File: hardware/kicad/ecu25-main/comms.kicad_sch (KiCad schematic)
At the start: 19 parts, among them J10 Screw_Terminal_RS485, J9 Screw_Terminal_CAN, U11 M95M02-DR, U6 TJA1051T/3, U7 THVD1450

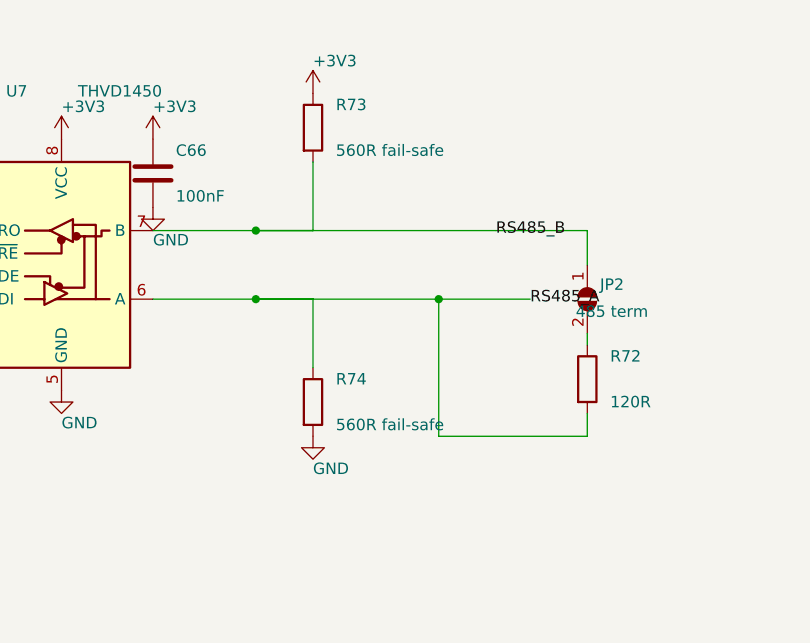
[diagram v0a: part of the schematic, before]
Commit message: Fix SME review findings: 3 critical, 6 major schematic faults
Critical:
- RON pin no longer shorted to GND (R4 moved off C3's column)
- LM2903 MPU comparator +/- inputs unmerged (separate route columns)
- Supercap charge diode D70 un-reversed (anode to +3V3)

Major:
- Buck UVLO divider restored (stray EN stub ended on C3 column = EN
  tied to +24V; stub removed)
- RS485 fail-safe bias polarity corrected (pull-up A, pull-down B)
- U8 spare op-amp unit placed and tied off (was floating on VREF die)
- Heartbeat LED DS1 un-reversed
- VREF_MID buffer dual feedback added (R93 DC path + C93 AC path)
- D80 value SMBJ33A -> SMBJ33CA (bidirectional, matches symbol)

Added netlist-level sweep check (shorted 2-pin devices, rail
membership) since the geometric tracer is blind to shorts closed
through power symbols across wire islands. Sweep: CLEAN, 0 issues.
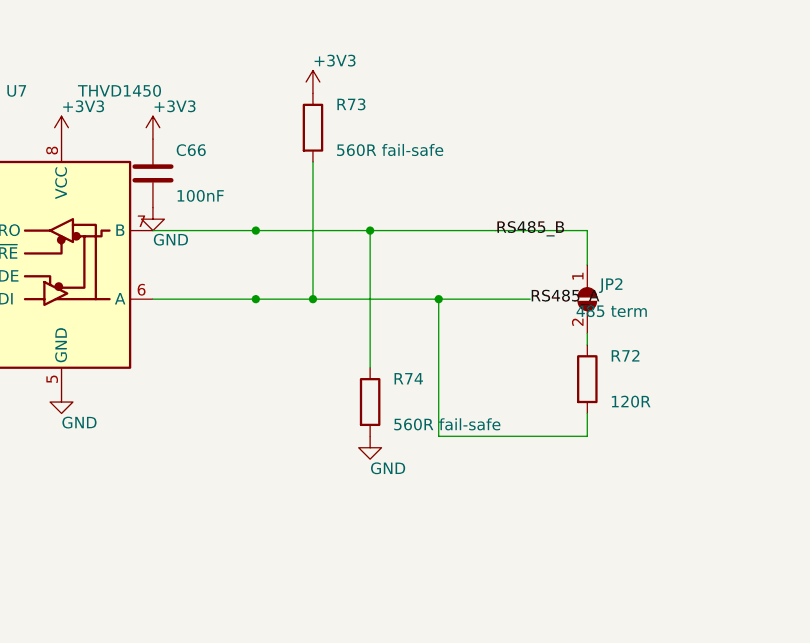
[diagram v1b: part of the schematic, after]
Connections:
- net RS485_A: now also R73.2; no longer R74.1
- net RS485_B: now also R74.1; no longer R73.2

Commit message: Assign footprints to all 299 components in schematic generator
- By-ref exceptions + per-symbol defaults + value rules (wattage/voltage classes)
- Field connectors: MKDS-3 for battery/AC/CT/relay terminals, MKDS-1,5 for signal
- Q1 reverse-protection FET: Q_PMOS_GSD -> Q_PMOS_GDS + TO-252-2 (DPAK pad
  numbering 1=G 2=D 3=S; GSD variant would swap D/S in the netlist), part
  SQD50P06-15L
- Verified: all footprint files exist in KiCad 7 libs, all symbol pin numbers
  present in footprint pads, netlist sweep still clean
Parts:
- C65, C66, C67, C70: footprint (none) -> Capacitor_SMD:C_0603_1608Metric
- J10, J9: footprint (none) -> TerminalBlock_Phoenix:TerminalBlock_Phoenix_MKDS-1,5-3-5.08_1x03_P5.08mm_Horizontal
- JP1, JP2: footprint (none) -> Jumper:SolderJumper-2_P1.3mm_Open_RoundedPad1.0x1.5mm
- R72, R73, R74, R78, R79, R95, R96, R97: footprint (none) -> Resistor_SMD:R_0603_1608Metric
- U11, U6, U7: footprint (none) -> Package_SO:SOIC-8_3.9x4.9mm_P1.27mm
